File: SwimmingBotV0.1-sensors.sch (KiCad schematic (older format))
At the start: 6 parts, among them U6 MPU-9250, U7 MICRO-SD

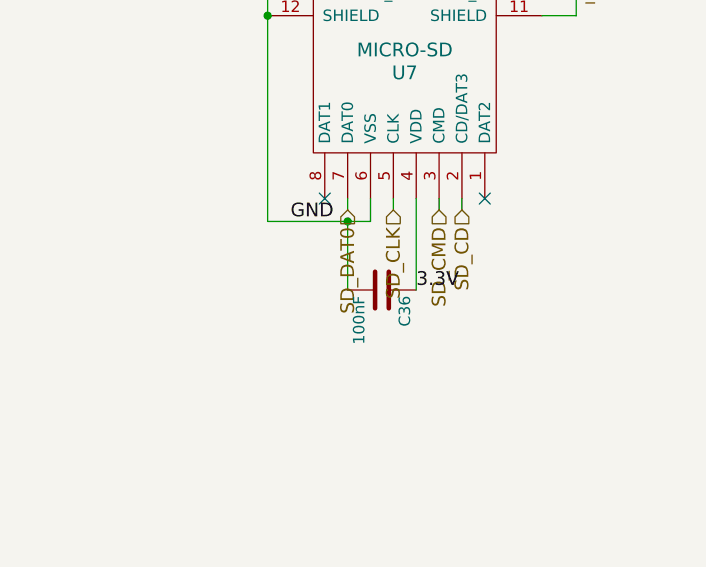
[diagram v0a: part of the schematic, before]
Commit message: potentially done with parts removal and reselection, on to pcb layout
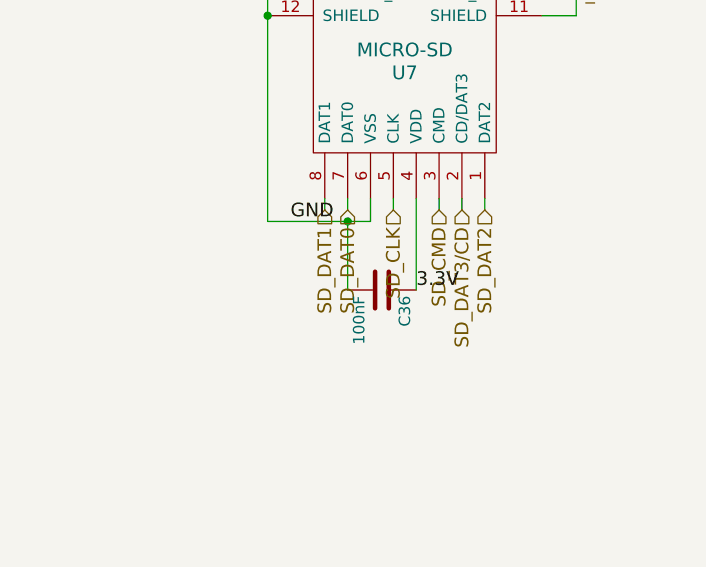
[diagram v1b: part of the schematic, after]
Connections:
- net SD_DAT2: now reaches U7.1 (DAT2)
- net SD_DAT1: now reaches U7.8 (DAT1)
- net SD_CD renamed SD_DAT3/CD
- no-connect marks 12 -> 10
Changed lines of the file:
@@
 $Descr A4 11693 8268
 encoding utf-8
-Sheet 8 8
+Sheet 6 8
 Title ""
 Date ""
@@
 	7000 2800 7000 2700
 Connection ~ 6550 1900
-NoConn ~ 7500 2700
-NoConn ~ 6800 2700
 Text Label 6650 2800 0    60   ~ 0
 GND
@@
 3.3V
 Text HLabel 7400 2750 3    60   Input ~ 0
-SD_CD
+SD_DAT3/CD
 Text HLabel 7300 2750 3    60   Input ~ 0
 SD_CMD
@@
 Text Notes 2550 1350 0    60   ~ 0
 AUX_ I2C lines can be communicated with\nautomagically by the mpu9250\nsaving processor time by consolidating reads
+Text HLabel 6800 2750 3    60   Input ~ 0
+SD_DAT1
+Text HLabel 7500 2750 3    60   Input ~ 0
+SD_DAT2
+Wire Wire Line
+	7500 2750 7500 2700
+Wire Wire Line
+	6800 2750 6800 2700
 $EndSCHEMATC
